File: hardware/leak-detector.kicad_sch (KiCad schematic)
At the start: 20 parts, among them J1 Conn_Atmel_ISP_TagConnect_TC2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, SW1 PTS810, U1 BMP581, U2 ATtiny25V

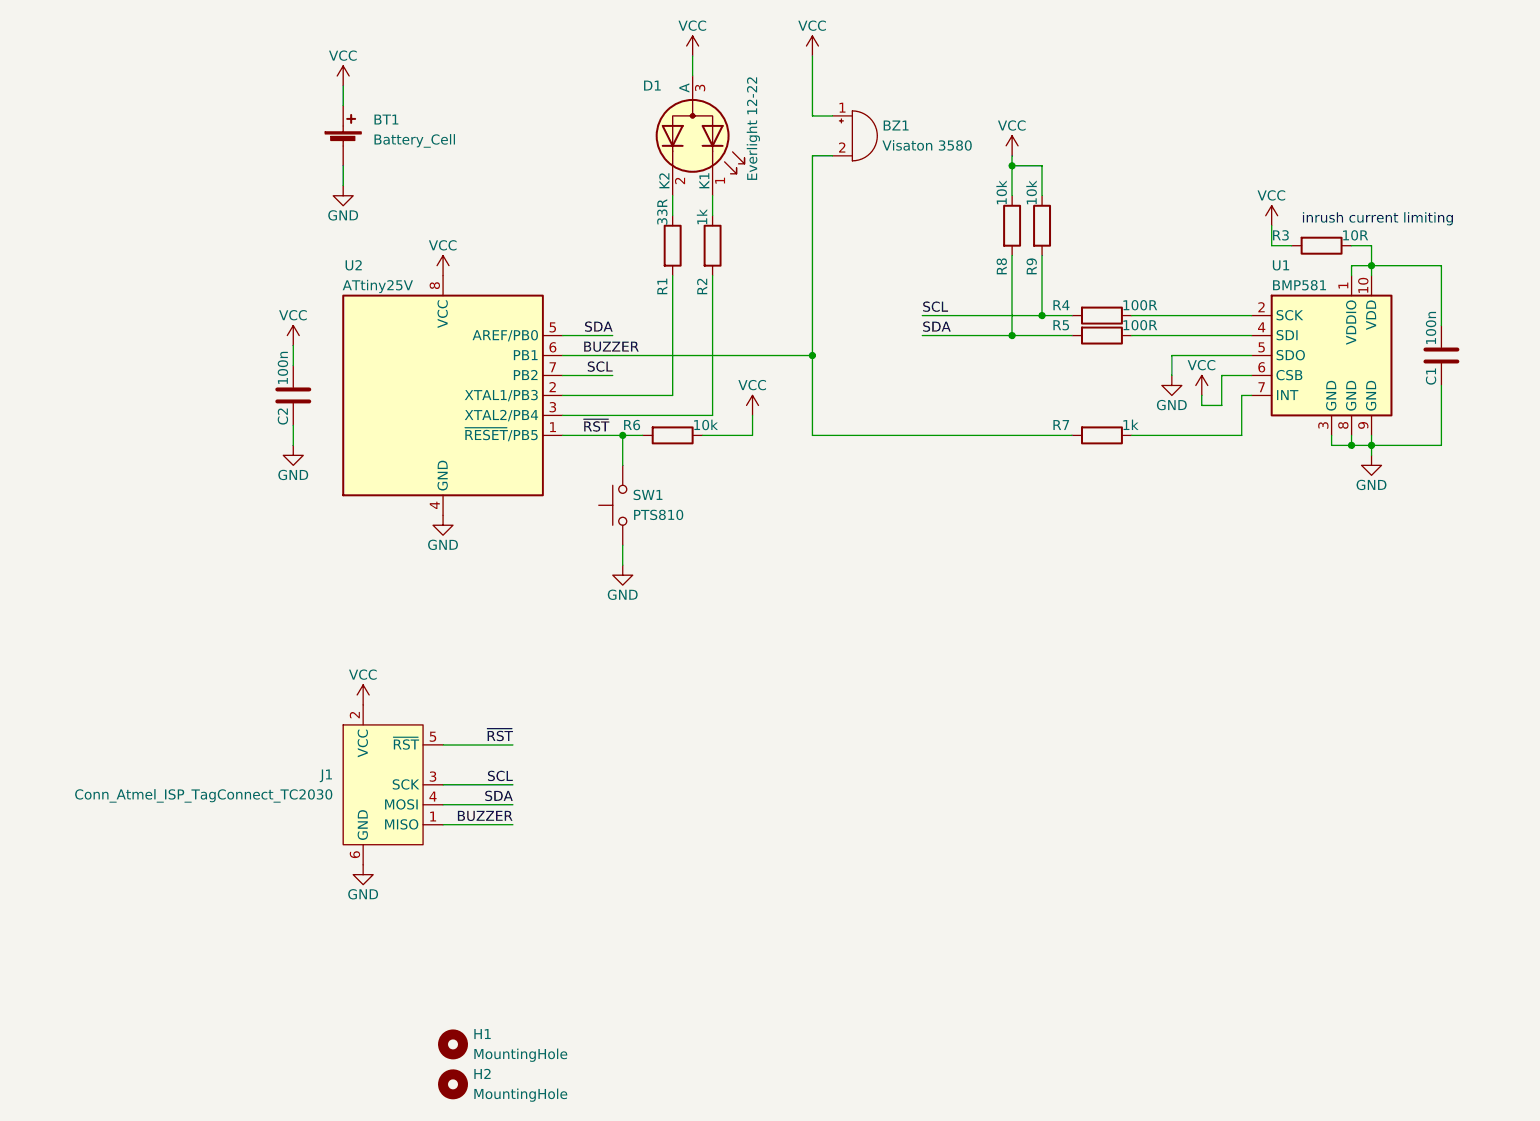
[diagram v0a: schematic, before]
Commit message: hardware: update to attiny412
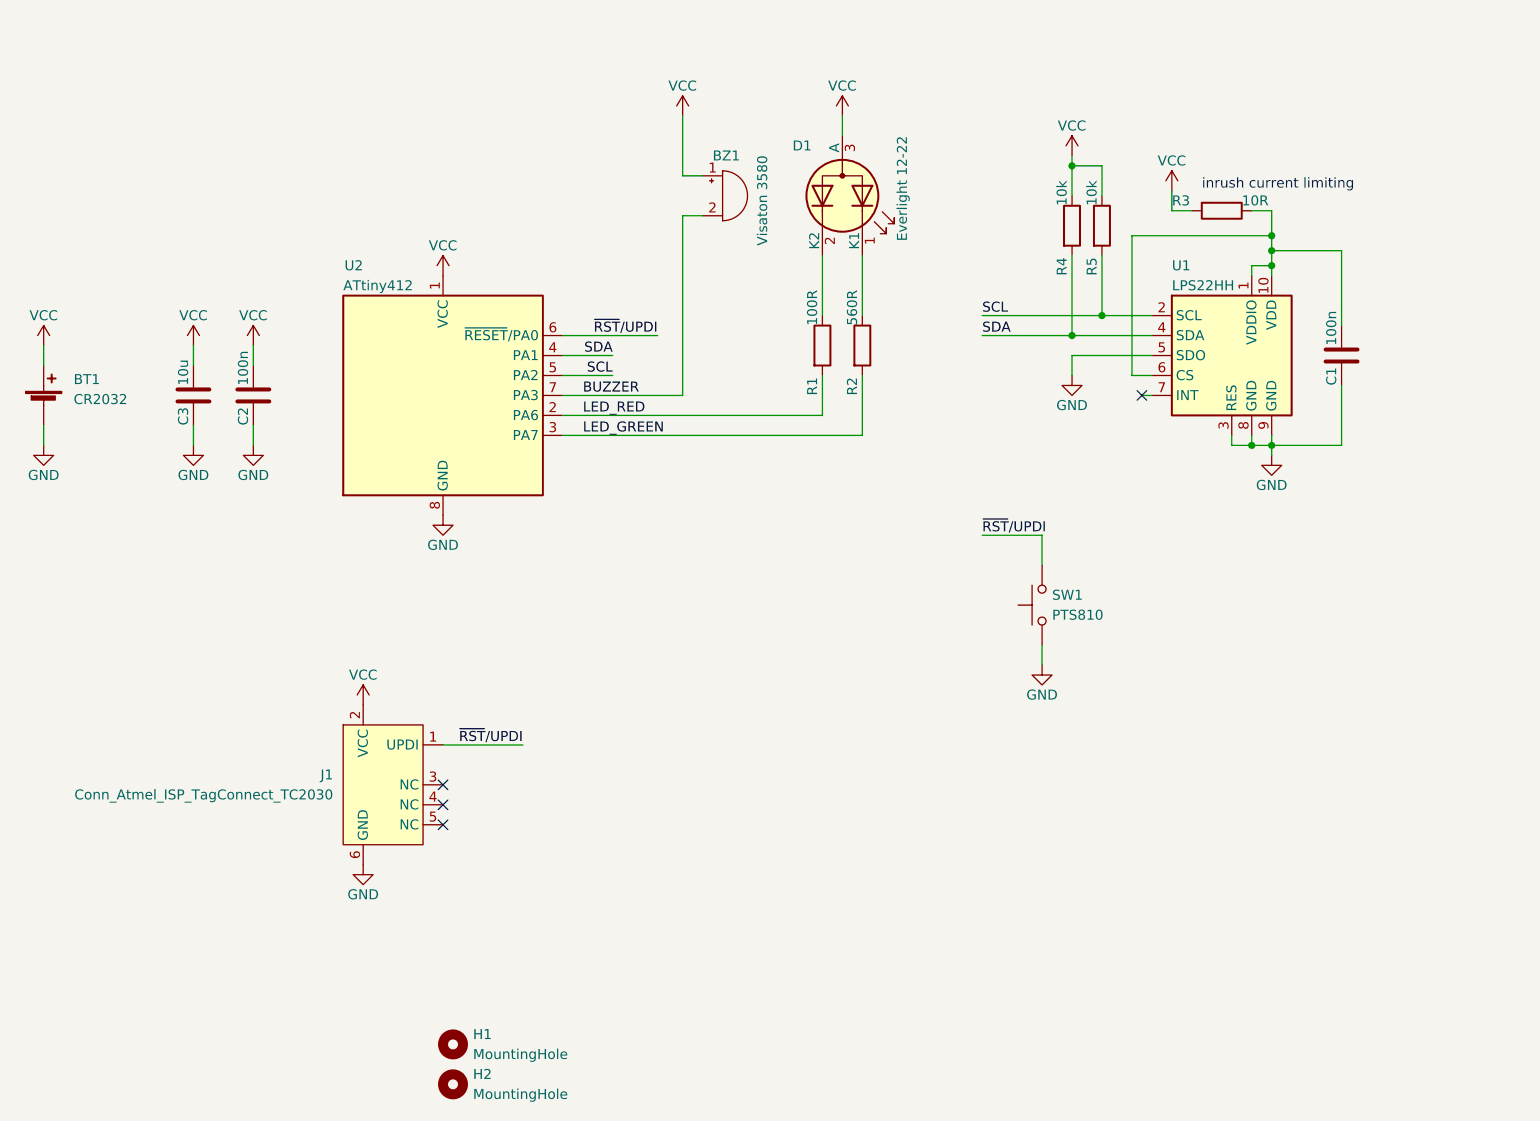
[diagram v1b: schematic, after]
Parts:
- removed R4, R5: 100R, Resistor_SMD:R_0603_1608Metric, symbol Device:R
- removed R6: 10k, Resistor_SMD:R_0603_1608Metric, symbol Device:R
- removed R7: 1k, Resistor_SMD:R_0603_1608Metric, symbol Device:R
- added C3: 10u, Capacitor_SMD:C_0805_2012Metric, symbol Device:C
- BT1: value Battery_Cell -> CR2032
- J1: symbol L_Connector:Conn_Atmel_ISP_TagConnect_TC2030 -> L_Connector:Conn_Atmel_UPDI_TagConnect_TC2030
- R1: value 33R -> 100R
- R2: value 1k -> 560R
- U1: value BMP581 -> LPS22HH; symbol L_Sensor_Pressure:BMP581 -> L_Sensor_Pressure:LPS22HH
- U2: value ATtiny25V -> ATtiny412; footprint Package_SO:SOIC-8_5.275x5.275mm_P1.27mm -> Package_SO:SOIC-8_3.9x4.9mm_P1.27mm; symbol MCU_Microchip_ATtiny:ATtiny25V-10S -> MCU_Microchip_ATtiny:ATtiny412-SS
- renumbered R8 to R4, R9 to R5
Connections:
- net BUZZER: now also U2.7 (PA3); no longer J1.1 (MISO), U2.6 (PB1)
- net GND: now also U2.8 (GND), C3.2; no longer U2.4 (GND)
- net SCL: now also U1.2 (SCL), U2.5 (PA2); no longer J1.3 (SCK), U2.7 (PB2)
- net SDA: now also U1.4 (SDA), U2.4 (PA1); no longer J1.4 (MOSI), U2.5 (AREF/PB0)
- net VCC: now also U2.1 (VCC), C3.1; no longer U1.6 (CSB), U2.8 (VCC)
- net LED_RED: now reaches R1.2, U2.2 (PA6)
- net at C1.1, R3.1, U1.1 (VDDIO)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: now also U1.6 (CS)
- net LED_GREEN: now reaches R2.2, U2.3 (PA7)
- removed net ~{RST}: J1.5 (~{RST}), SW1.2, U2.1 (~{RESET}/PB5)
- new net ~{RST}/UPDI: J1.1 (UPDI), SW1.2, U2.6 (~{RESET}/PA0)
- no-connect marks 0 -> 4
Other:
- moved on the sheet: BT1, BZ1, C1, C2, D1, R1, R2, R3, R4, R5, U1
